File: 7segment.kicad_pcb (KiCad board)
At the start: 2 copper layers, 111.8 x 205.7 mm, 70 parts, among them J1 Conn_01x03, J2 Conn_01x03

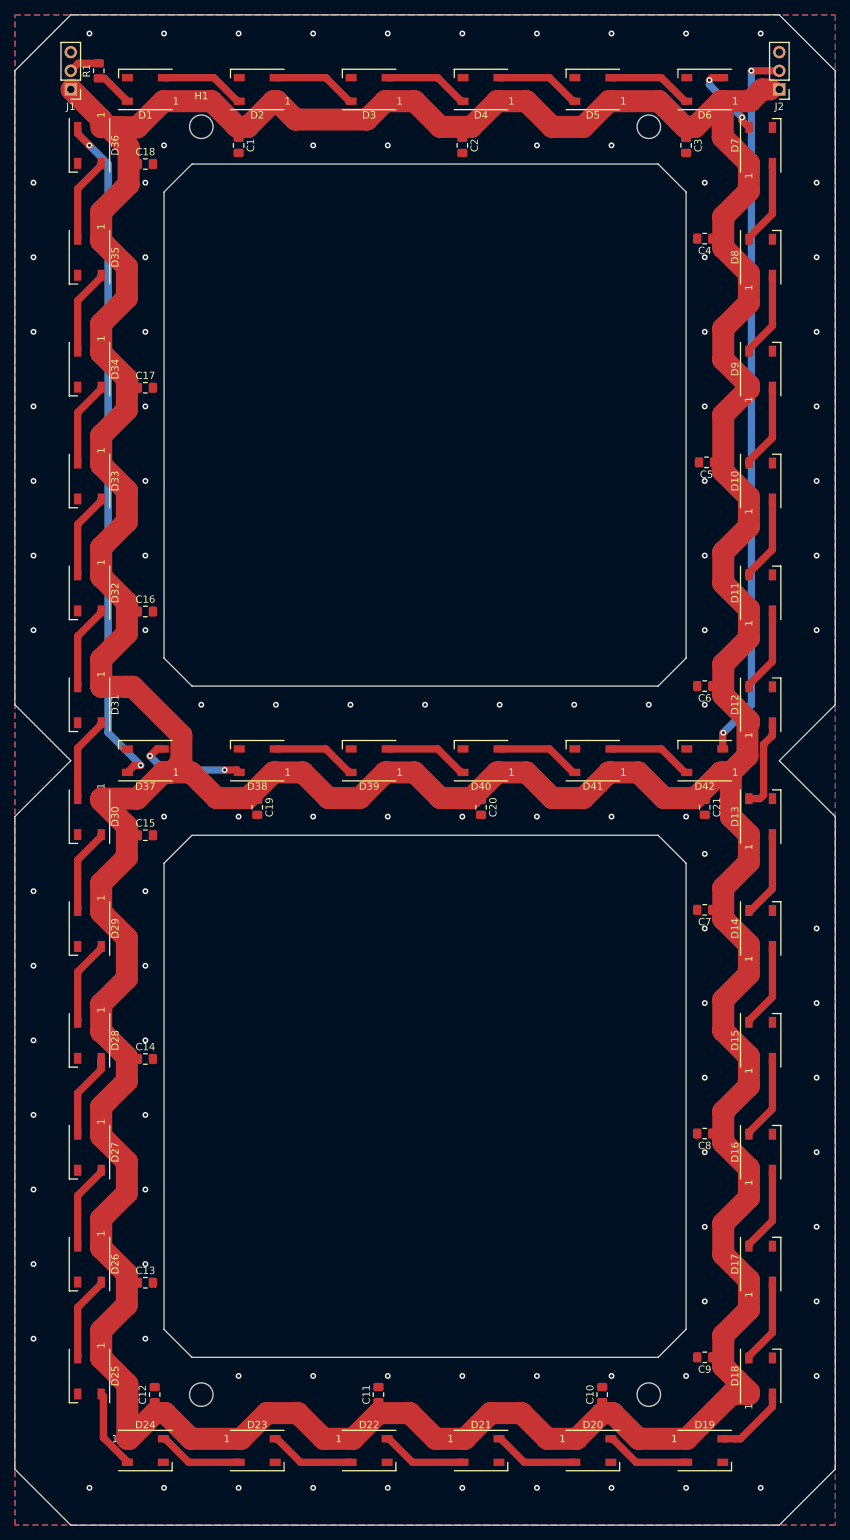
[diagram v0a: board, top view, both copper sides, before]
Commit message: Add labels to connectors
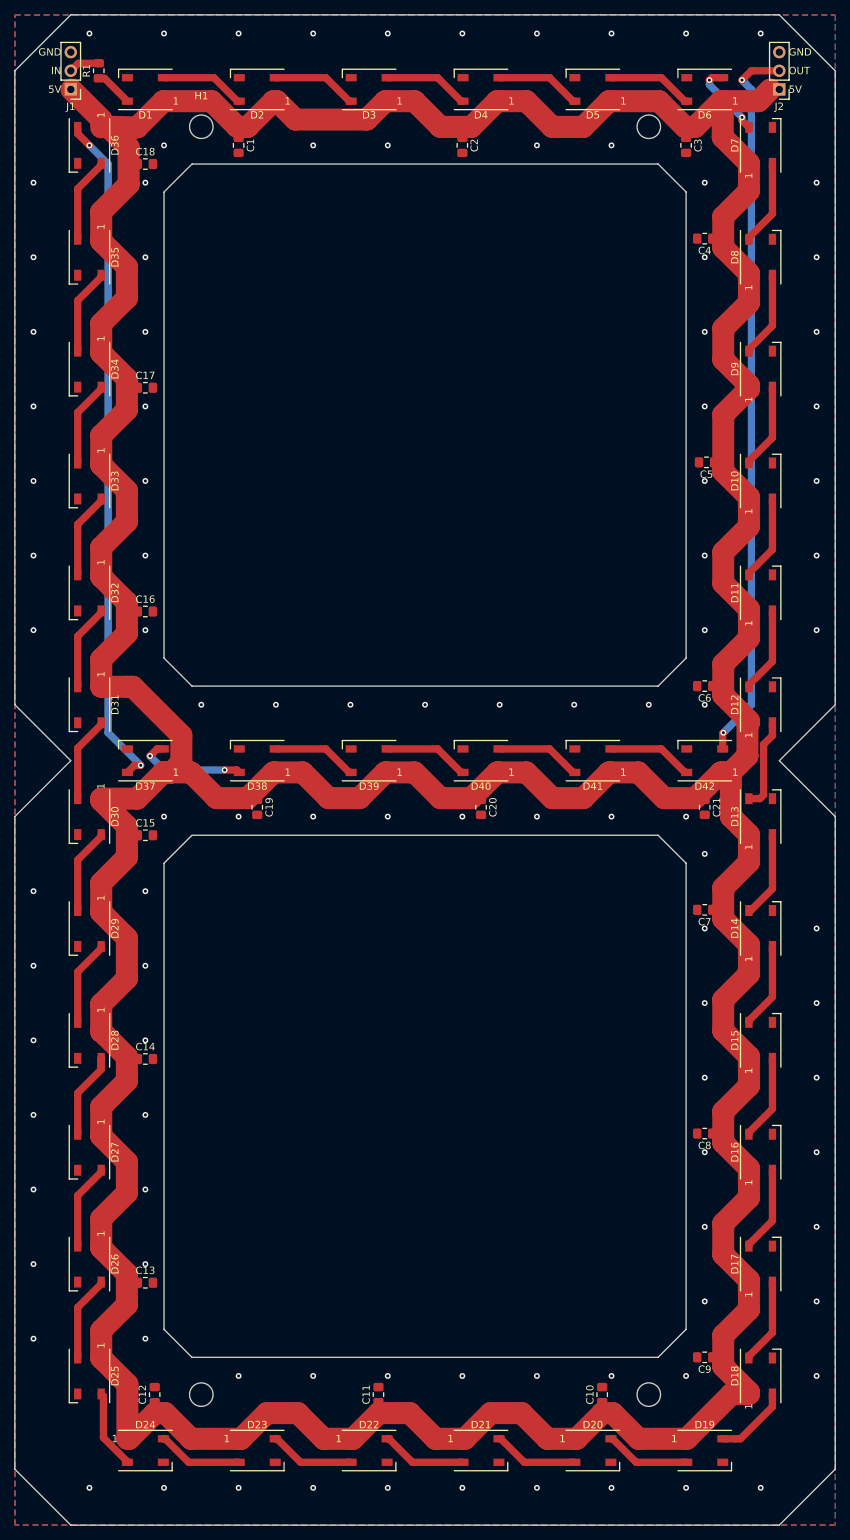
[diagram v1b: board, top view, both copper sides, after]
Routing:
- net Net-(D42-Pad2): track 97.8 -> 98.9 mm
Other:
- board text added: "5V"
- board text added: "GND"
- board text added: "IN"
- board text added: "OUT"
